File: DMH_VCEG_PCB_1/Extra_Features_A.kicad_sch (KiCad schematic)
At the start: 35 parts, among them Q4 BC548, SW1 SW_DPDT_x2, U1 TL074, U3 40106, U4 CD4066BE, U8 TL074

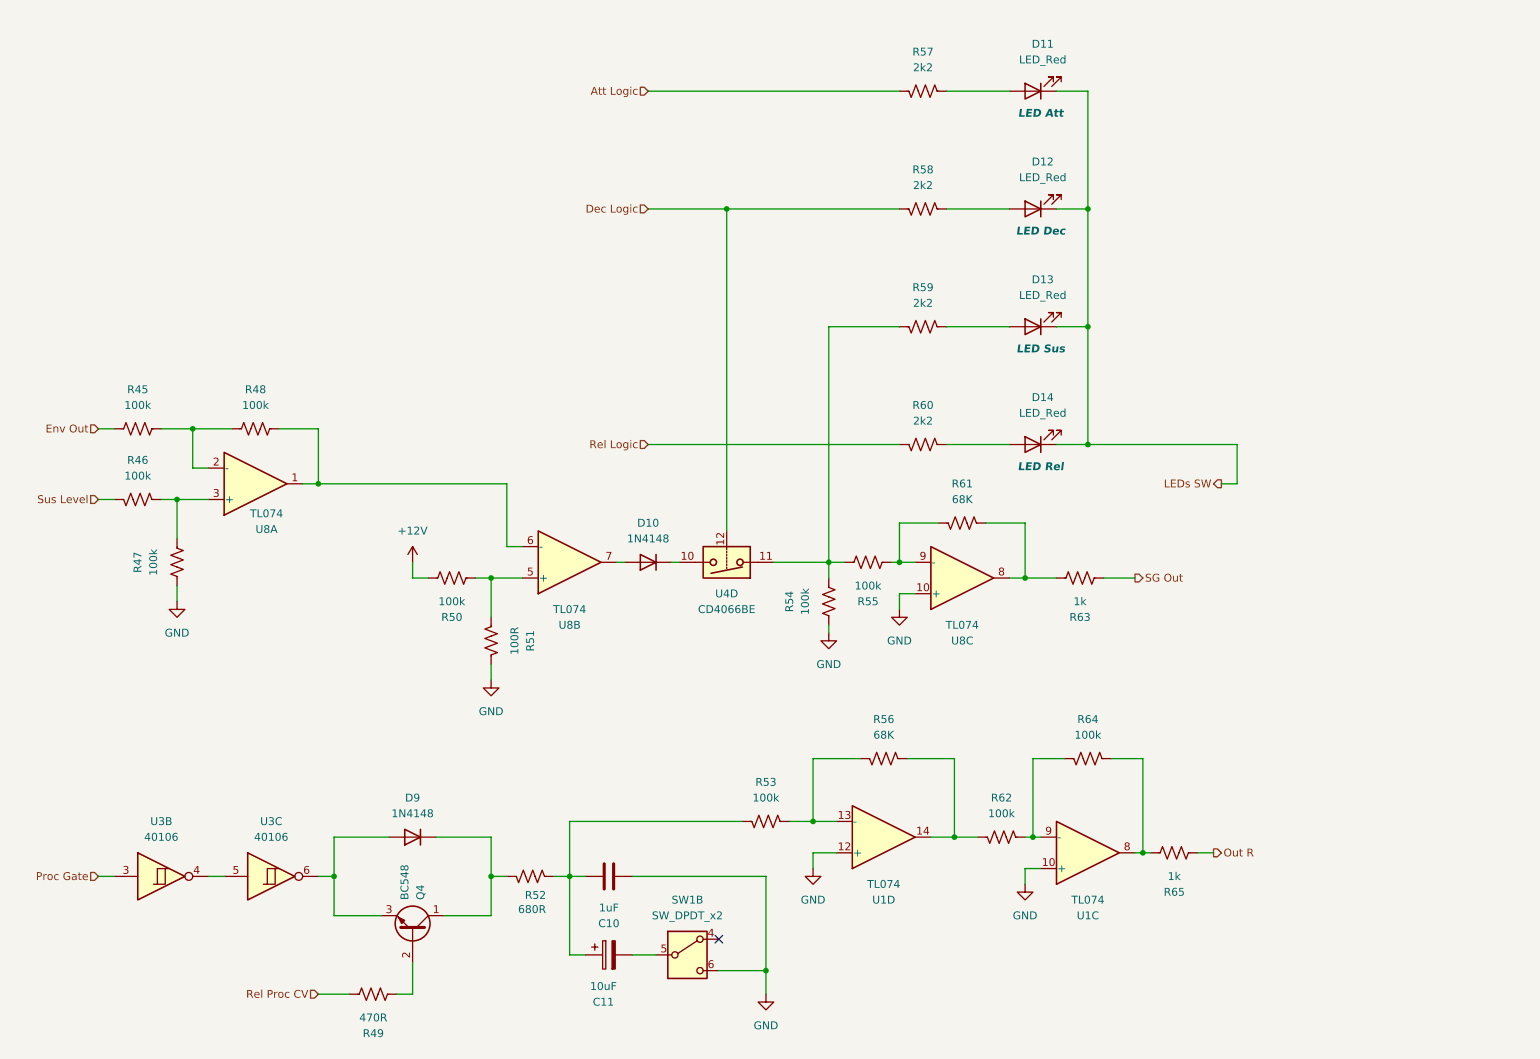
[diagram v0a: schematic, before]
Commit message: Updated SG Out circuit
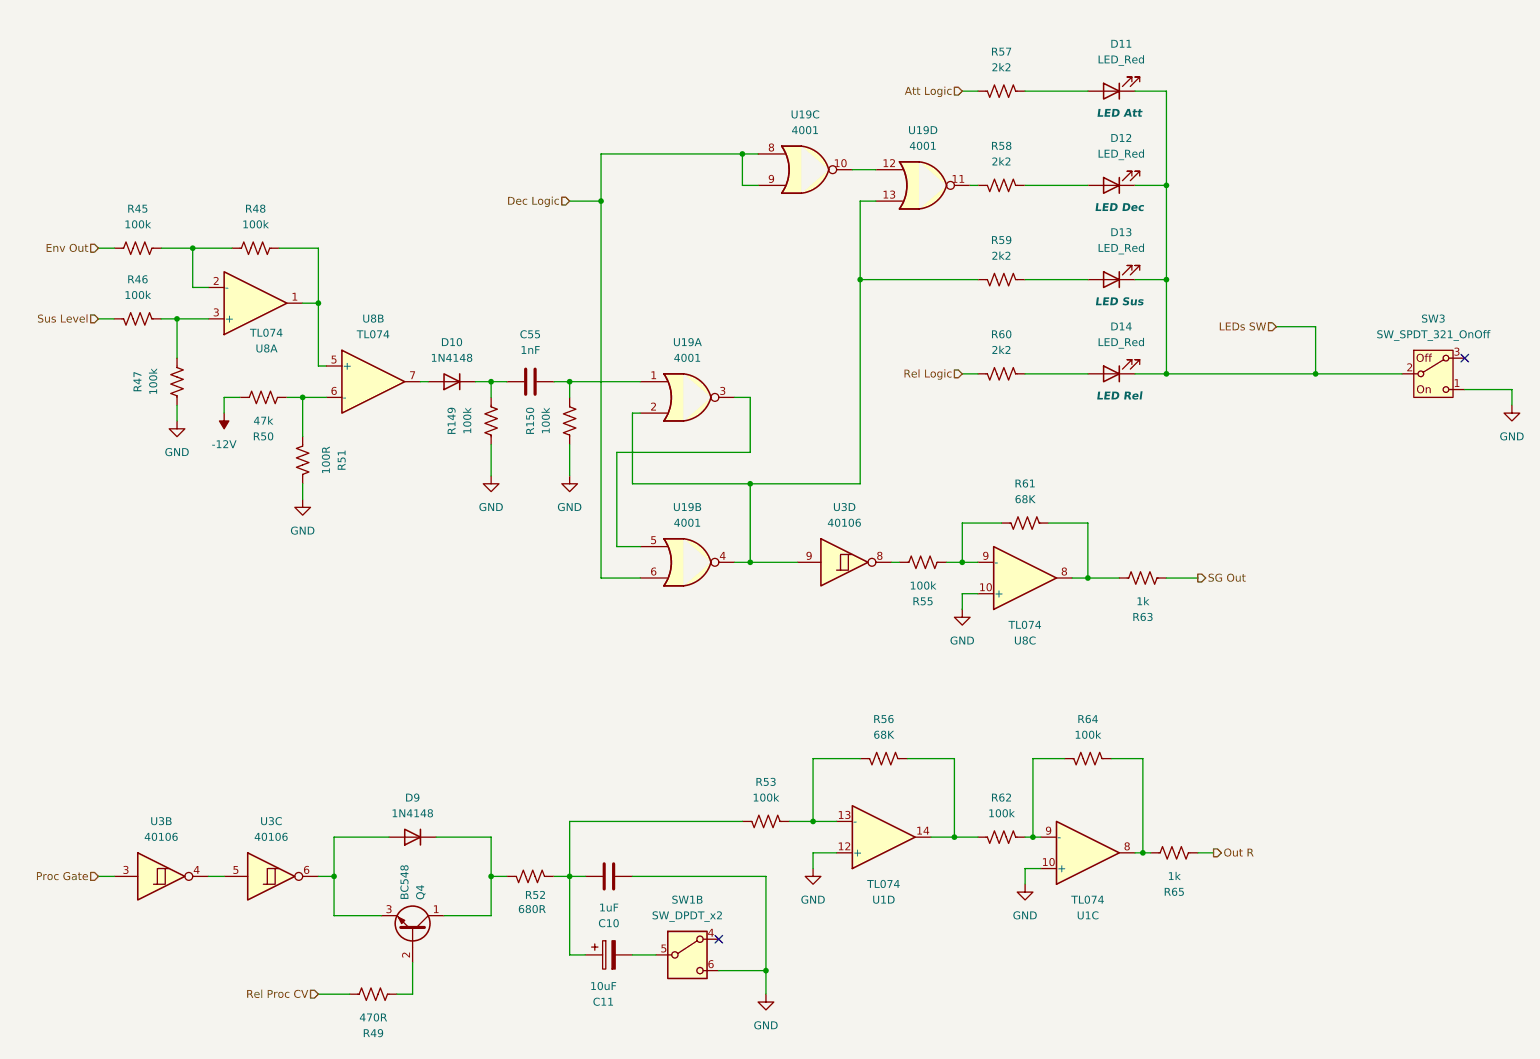
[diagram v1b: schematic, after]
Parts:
- removed R54: 100k, Resistor_THT:R_Axial_DIN0207_L6.3mm_D2.5mm_P7.62mm_Horizontal, symbol Device:R_US
- removed U4: CD4066BE, Package_DIP:DIP-14_W7.62mm, symbol Analog_Switch:CD4066BE
- added C55: 1nF, Capacitor_THT:C_Disc_D4.3mm_W1.9mm_P5.00mm, symbol Device:C
- added R149, R150: 100k, Resistor_THT:R_Axial_DIN0207_L6.3mm_D2.5mm_P7.62mm_Horizontal, symbol Device:R_US
- added SW3: SW_SPDT_321_OnOff, SynthStuff:Toggle_Switch_TE, symbol SynthStuff:SW_SPDT_321_OnOff
- added U19: 4001, Package_DIP:DIP-14_W7.62mm_Socket, symbol 4xxx:4001
- added unit 4 of U3
- R50: value 100k -> 47k
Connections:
- net Dec Logic: now also U19.6, U19.8, U19.9; no longer R58.1
- net GND: now also R149.2, R150.2, SW3.1 (C)
- net LEDs SW: now also SW3.2 (B)
- net at D10.1 (K): now also C55.1, R149.1
- net at R59.1: now also U19.13, U19.2, U19.4, U3.9; no longer R55.1
- net at R48.1, U8.1: now also U8.5 (+); no longer U8.6 (-)
- net at R50.2, R51.1: now also U8.6 (-); no longer U8.5 (+)
- net +12V renamed -12V
- new net: C55.2, R150.1, U19.1
- new net: U19.3, U19.5
- new net: R55.1, U3.8
- new net: R58.1, U19.11
- new net: U19.10, U19.12
- no-connect marks 1 -> 2
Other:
- moved on the sheet: D10, D11, D12, D13, D14, R45, R46, R47, R48, R50, R51, R55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

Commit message: Added Loop circuit
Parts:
- added C59: 1nF, Capacitor_THT:C_Disc_D4.3mm_W1.9mm_P5.00mm, symbol Device:C
- added D27: 1N4148, Diode_THT:D_DO-35_SOD27_P7.62mm_Horizontal, symbol Diode:1N4148
- added R151, R152, R153: 100k, Resistor_THT:R_Axial_DIN0207_L6.3mm_D2.5mm_P7.62mm_Horizontal, symbol Device:R_US
- added R154: 10k, Resistor_THT:R_Axial_DIN0207_L6.3mm_D2.5mm_P7.62mm_Horizontal, symbol Device:R_US
- added SW4: SW_SPDT_321_OnOff, SynthStuff:Toggle_Switch_TE, symbol SynthStuff:SW_SPDT_321_OnOff
- added U21: TL072, Package_DIP:DIP-8_W7.62mm, symbol Amplifier_Operational:TL072
- R149: value 100k -> 10k
- SW1: Function (none) -> Long A
- SW3: Function (none) -> LEDs On/Off
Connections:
- net Env Out: now also U21.2 (-)
- net GND: now also R153.2, R154.2
- new net: D27.2 (A), R151.1, U21.1
- new net: R151.2, R152.1, R153.1, U21.3 (+)
- new net: C59.1, D27.1 (K), R154.1
- new net: C59.2, SW4.2 (B)
- new net +12V: R152.2
- new net Loop: SW4.1 (C)
- no-connect marks 2 -> 3

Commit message: PCB 1 ready for placement
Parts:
- removed U21: TL072, Package_DIP:DIP-8_W7.62mm, symbol Amplifier_Operational:TL072
- added J22, J23: Conn_01x10_PinHeader, symbol SynthStuff:Conn_01x10_PinHeader
- added unit 4 of U8
- U19: footprint (none) -> Package_DIP:DIP-14_W7.62mm_Socket
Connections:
- net Att Logic: now also J22.8 (Pin_8)
- net Dec Logic: now also J22.9 (Pin_9)
- net Env Out: now also U8.13 (-)
- net Loop: now also J23.3 (Pin_3)
- net Proc Gate: now also J23.4 (Pin_4)
- net Rel Logic: now also J22.10 (Pin_10)
- net Rel Proc CV: now also J23.6 (Pin_6)
- net SG Out: now also J23.9 (Pin_9)
- net Sus Level: now also J23.10 (Pin_10)
- net at R59.1, U19.13, U19.2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: now also J23.8 (Pin_8)
- net at D27.2 (A), R151.1: now also U8.14
- net at R151.2, R152.1, R153.1: now also U8.12 (+)
- net at D9.2 (A), Q4.3 (E), U3.6: now also J23.5 (Pin_5)
- net at R55.1, U3.8: now also J23.7 (Pin_7)
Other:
- note added: "PCB 1"
- moved on the sheet: C10, C11, D9, Q4, R49, R52, R53, R55, R56, R61, R62, R63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

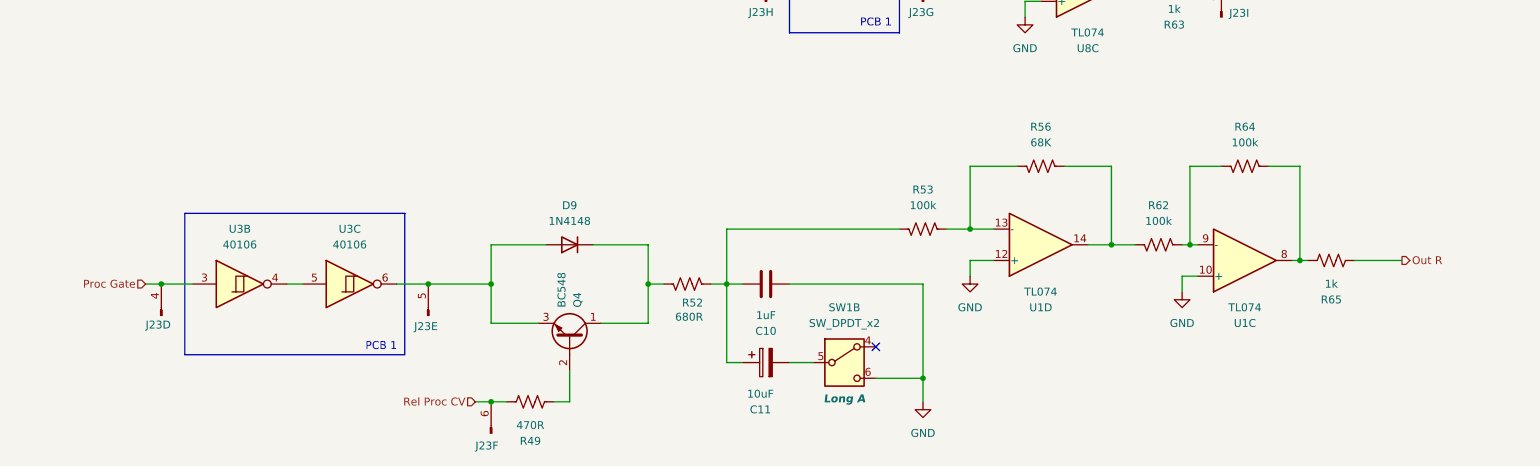
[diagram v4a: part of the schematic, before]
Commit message: Placed ICs and pin headers on PCB 2
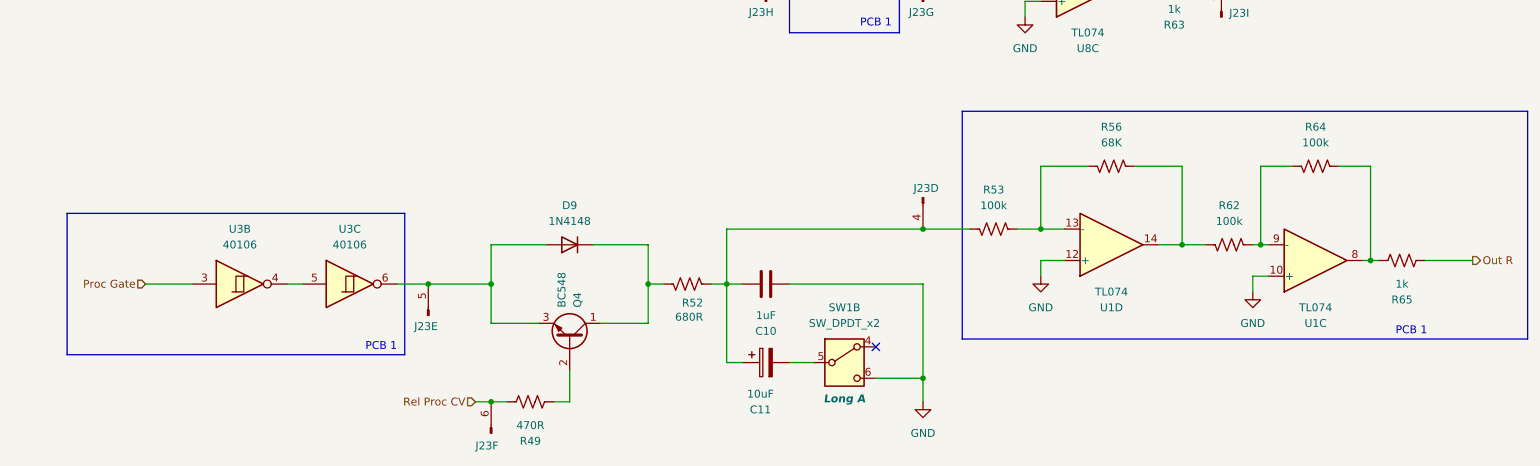
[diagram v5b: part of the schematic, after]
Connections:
- net Proc Gate: no longer J23.4 (Pin_4)
- net at C10.1, C11.1, R52.1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: now also J23.4 (Pin_4)
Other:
- moved on the sheet: R53, R56, R62, R64, R65, U1C, U1D

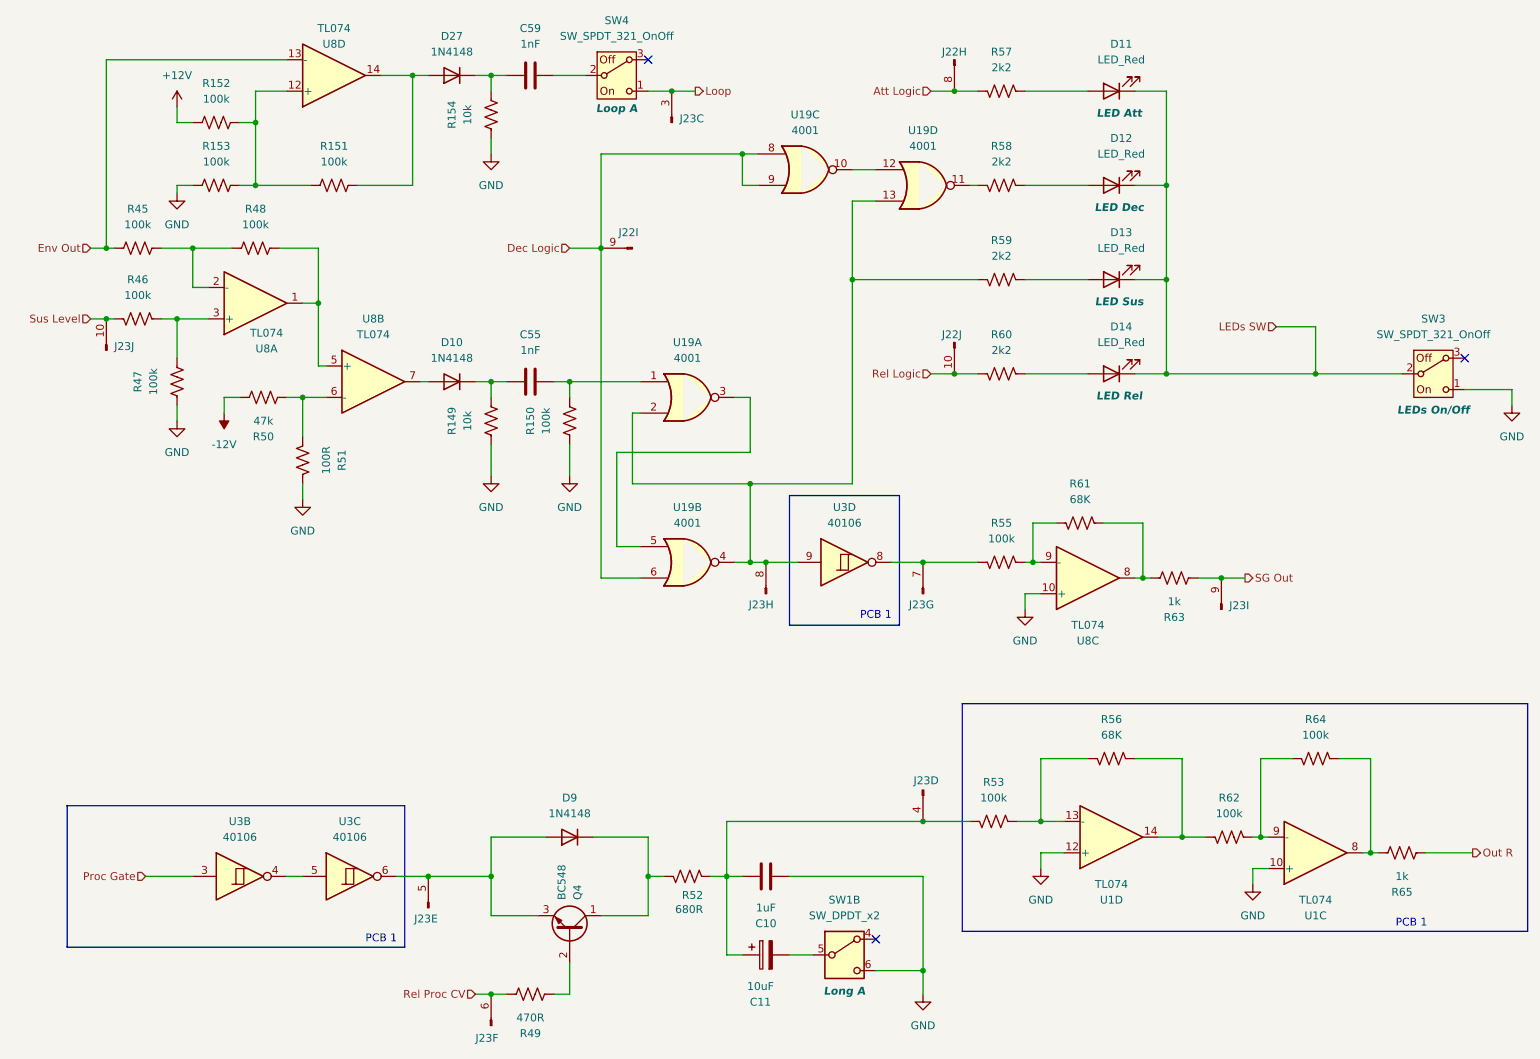
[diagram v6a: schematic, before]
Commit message: Copied Manual Gate circuit to PCB 1 schematic
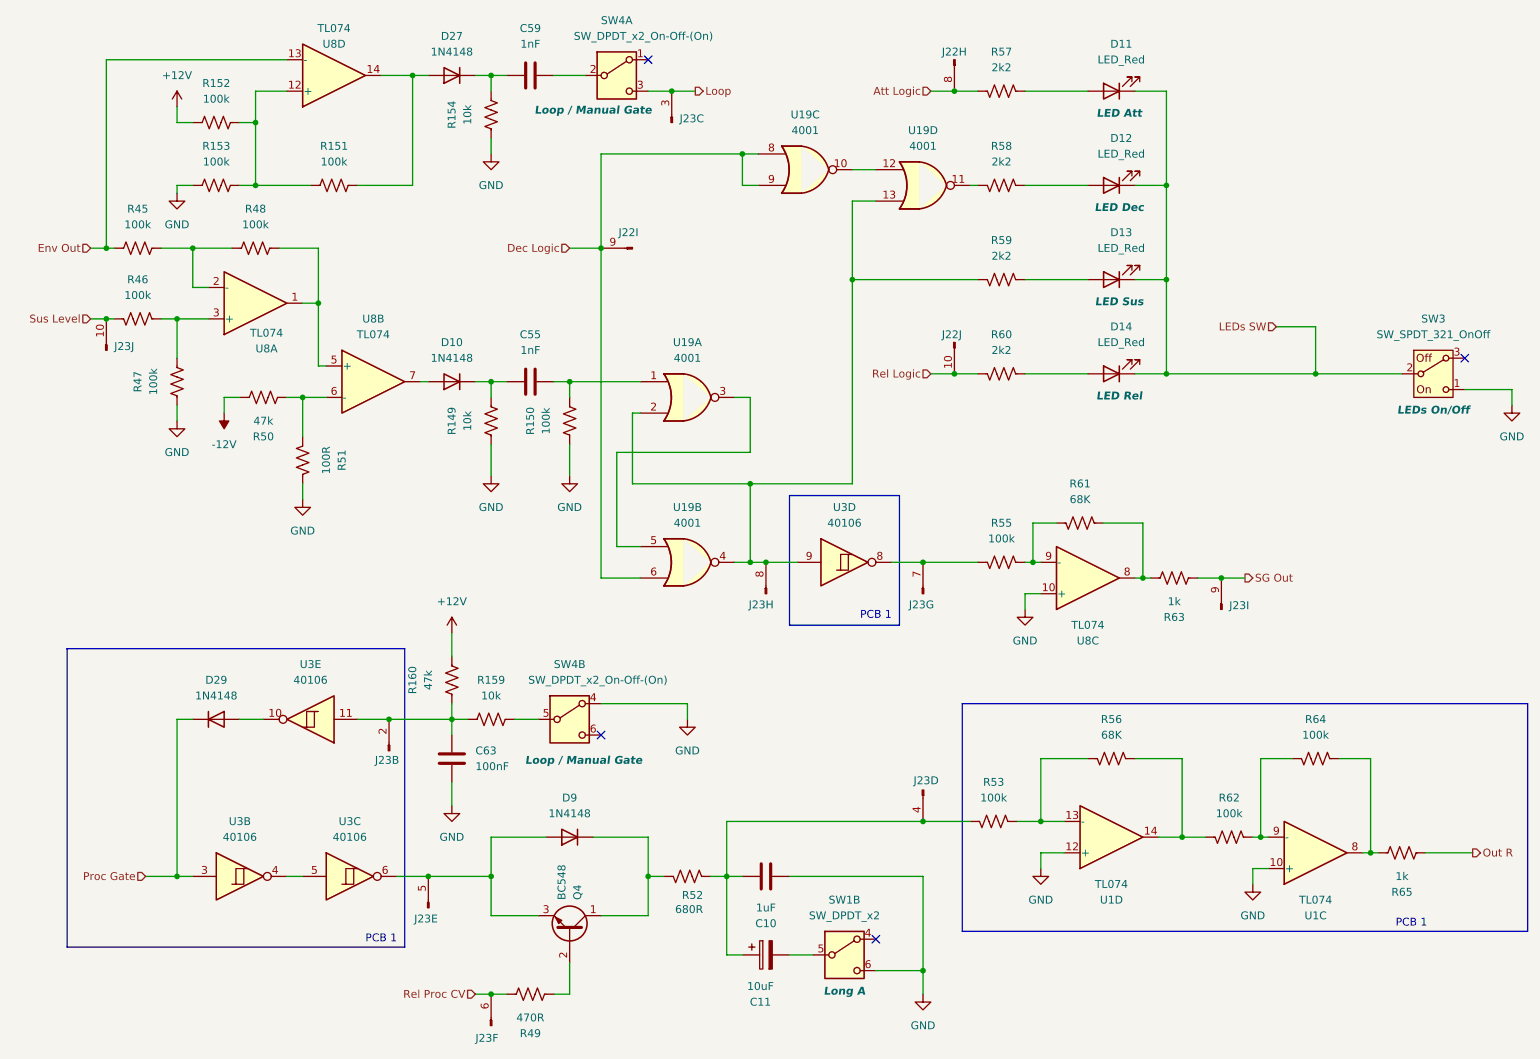
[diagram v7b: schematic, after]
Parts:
- removed SW4: SW_SPDT_321_OnOff, SynthStuff:Toggle_Switch_TE, symbol SynthStuff:SW_SPDT_321_OnOff
- added C63: 100nF, Capacitor_THT:C_Disc_D4.3mm_W1.9mm_P5.00mm, symbol Device:C
- added D29: 1N4148, Diode_THT:D_DO-35_SOD27_P7.62mm_Horizontal, symbol Diode:1N4148
- added unit 2 of J23
- added R159: 10k, Resistor_THT:R_Axial_DIN0207_L6.3mm_D2.5mm_P7.62mm_Horizontal, symbol Device:R_US
- added R160: 47k, Resistor_THT:R_Axial_DIN0207_L6.3mm_D2.5mm_P7.62mm_Horizontal, symbol Device:R_US
- added SW4: SW_DPDT_x2_On-Off-(On), symbol Switch:SW_DPDT_x2
- added unit 5 of U3
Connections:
- net +12V: now also R160.1
- net GND: now also C63.2, SW4.4 (A)
- net Loop: now also SW4.3 (C)
- net Proc Gate: now also D29.1 (K)
- net at C59.2: now also SW4.2 (B)
- new net: R159.1, SW4.5 (B)
- new net: C63.1, J23.2 (Pin_2), R159.2, R160.2, U3.11
- new net: D29.2 (A), U3.10
- no-connect marks 3 -> 4
